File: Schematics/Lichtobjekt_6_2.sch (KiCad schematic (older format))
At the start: 66 parts, among them IC1 STM32F10XCXT6, IC3 MCP1703DB 3.0V, J1 22-27-2031-03, J2 22-?-0227-2021, J3 22-?-0227-2021, J4 22-?-0227-2021, J5 22-?-0227-2021, Q3 IRLML6402, Q4 BSS138, Q5 BSS84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

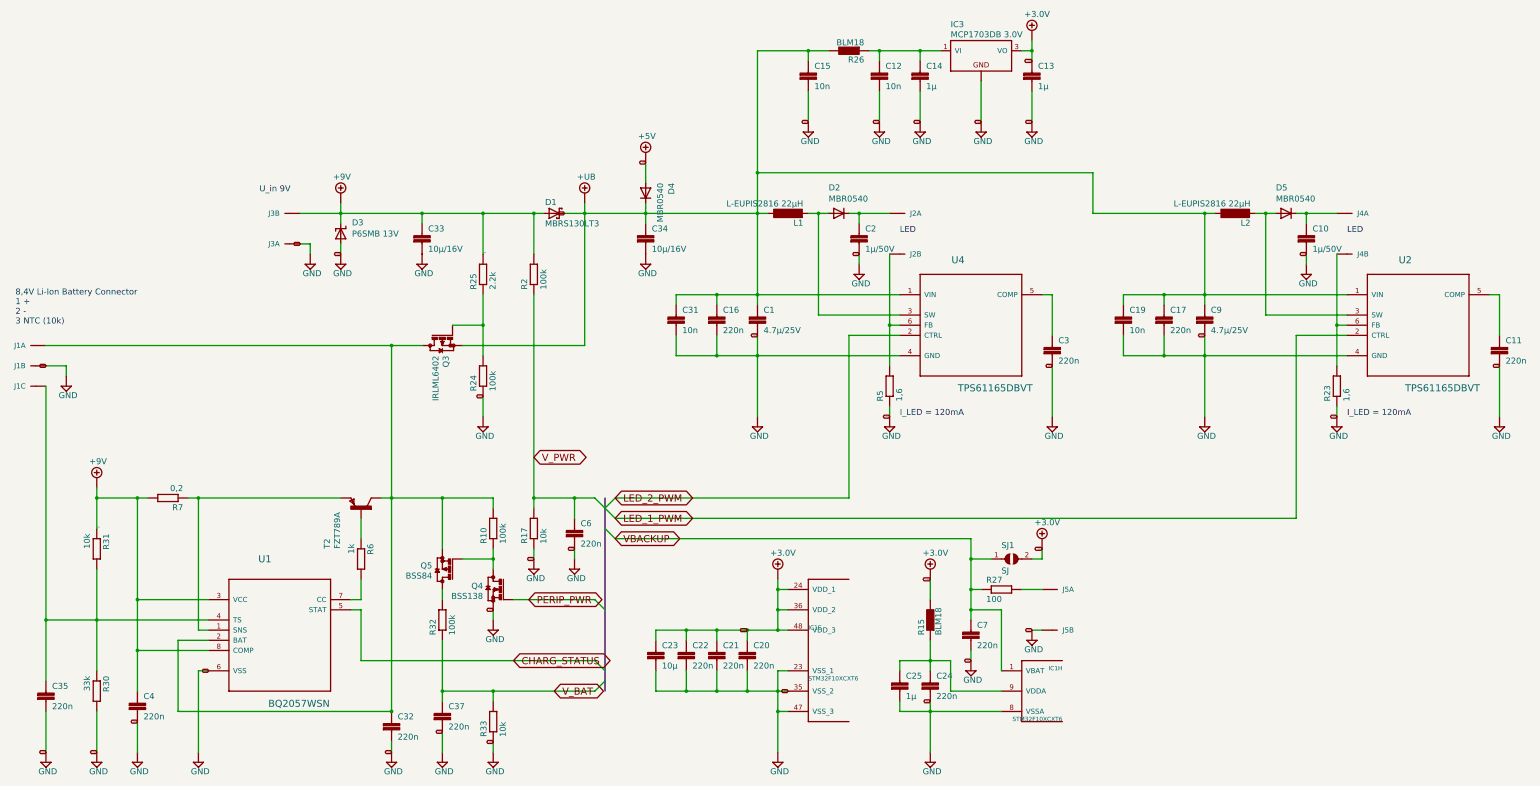
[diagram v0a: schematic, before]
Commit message: version of PCB produced first version to show basic functionality incl. remote and serial monitor output
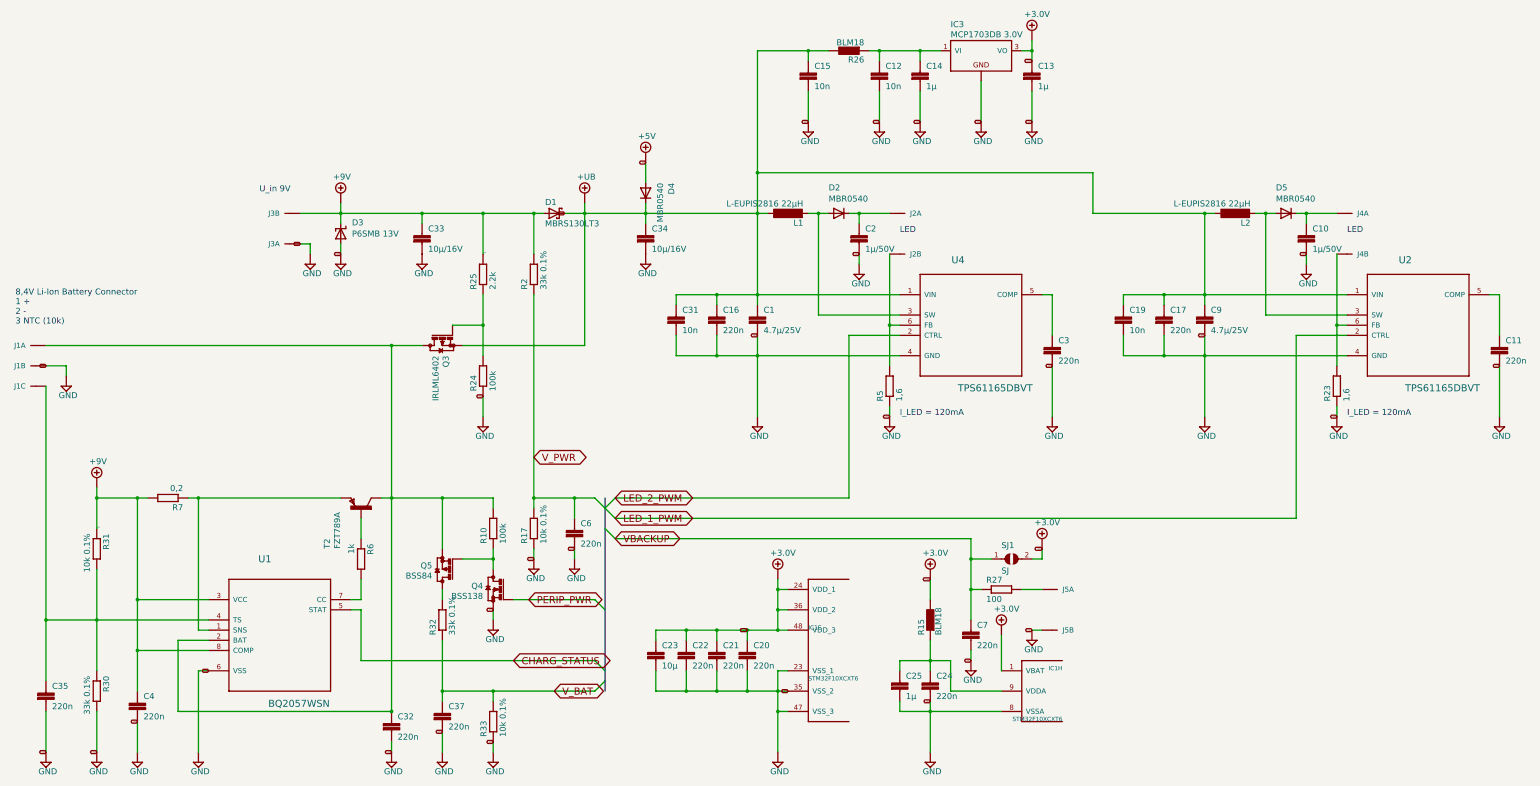
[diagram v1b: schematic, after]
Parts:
- R17, R31, R33: value 10k -> 10k 0.1%
- R2, R32: value 100k -> 33k 0.1%
- R30: value 33k -> 33k 0.1%
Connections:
- net VBACKUP: no longer IC1.1 (VBAT)
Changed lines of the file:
@@
 	7200 5900 10700 5900
 Wire Wire Line
-	10700 6600 10700 6700
-Wire Wire Line
-	10700 6600 10700 6400
-Wire Wire Line
 	10700 6400 10800 6400
-Wire Wire Line
-	11000 6600 10700 6600
-Wire Wire Line
-	11000 7200 11000 6600
 Wire Wire Line
 	10700 6400 10700 6100
@@
 Text GLabel 7200 5900 2    70   BiDi ~ 0
 VBACKUP
-Connection ~ 10700 6600
 Connection ~ 10700 6400
 Connection ~ 10700 6100
@@
 AR Path="/5FF63D6E/E60BDCA2" Ref="R30"  Part="1"
 F 0 "R30" H 1950 7459 59  0000 L BNN
-F 1 "33k" H 1950 7270 59  0000 L BNN
+F 1 "33k 0.1%" H 1950 7270 59  0000 L BNN
 F 2 "Lichtobjekt 6:R0805" H 2100 7400 50  0001 C CNN
 F 3 "" H 2100 7400 50  0001 C CNN
@@
 AR Path="/5FF63D6E/941D0DBE" Ref="R31"  Part="1"
 F 0 "R31" H 1950 6059 59  0000 L BNN
-F 1 "10k" H 1950 5870 59  0000 L BNN
+F 1 "10k 0.1%" H 1950 5870 59  0000 L BNN
 F 2 "Lichtobjekt 6:R0805" H 2100 6000 50  0001 C CNN
 F 3 "" H 2100 6000 50  0001 C CNN
@@
 AR Path="/5FF63D6E/94142453" Ref="R32"  Part="1"
 F 0 "R32" H 5350 6759 59  0000 L BNN
-F 1 "100k" H 5350 6570 59  0000 L BNN
+F 1 "33k 0.1%" H 5350 6570 59  0000 L BNN
 F 2 "Lichtobjekt 6:R0805" H 5500 6700 50  0001 C CNN
 F 3 "" H 5500 6700 50  0001 C CNN
@@
 AR Path="/5FF63D6E/533B5267" Ref="R33"  Part="1"
 F 0 "R33" H 5850 7759 59  0000 L BNN
-F 1 "10k" H 5850 7570 59  0000 L BNN
+F 1 "10k 0.1%" H 5850 7570 59  0000 L BNN
 F 2 "Lichtobjekt 6:R0805" H 6000 7700 50  0001 C CNN
 F 3 "" H 6000 7700 50  0001 C CNN
@@
 AR Path="/5FF63D6E/B121436F" Ref="R2"  Part="1"
 F 0 "R2" H 6250 3359 59  0000 L BNN
-F 1 "100k" H 6250 3170 59  0000 L BNN
+F 1 "33k 0.1%" H 6250 3170 59  0000 L BNN
 F 2 "Lichtobjekt 6:R0805" H 6400 3300 50  0001 C CNN
 F 3 "" H 6400 3300 50  0001 C CNN
@@
 AR Path="/5FF63D6E/AC3F9421" Ref="R17"  Part="1"
 F 0 "R17" H 6250 5859 59  0000 L BNN
-F 1 "10k" H 6250 5670 59  0000 L BNN
+F 1 "10k 0.1%" H 6250 5670 59  0000 L BNN
 F 2 "Lichtobjekt 6:R0805" H 6400 5800 50  0001 C CNN
 F 3 "" H 6400 5800 50  0001 C CNN
@@
 Text Notes 14400 4700 0    59   ~ 0
 I_LED = 120mA
+Wire Wire Line
+	10700 6400 10700 6700
+$Comp
+L Lichtobjekt_6-eagle-import:+3.0V #SUPPLY?
+U 1 1 6081556A
+P 11000 6750
+AR Path="/6081556A" Ref="#SUPPLY?"  Part="1"
+AR Path="/5FF63D6E/6081556A" Ref="#SUPPLY0101"  Part="1"
+F 0 "#SUPPLY0101" H 11000 6750 50  0001 C CNN
+F 1 "+3.0V" H 10925 6875 59  0000 L BNN
+F 2 "" H 11000 6750 50  0001 C CNN
+F 3 "" H 11000 6750 50  0001 C CNN
+	1    11000 6750
+	1    0    0    -1
+$EndComp
+Wire Wire Line
+	11000 7200 11000 6850
 Wire Bus Line
 	7100 5500 7100 7400
